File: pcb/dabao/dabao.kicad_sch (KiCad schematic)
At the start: 67 parts, among them J1 Conn_01x05, J2 USB_C_Receptacle_USB2.0_16P, J3 Conn_01x04, J4 MagConn_01x04_Pin, J5 Conn_Battery, J7 Conn_01x04, J8 Display, SW1 SW_RESET, SW2 SW_POWER, U1 nice_nano, U2 MCP23017_SP

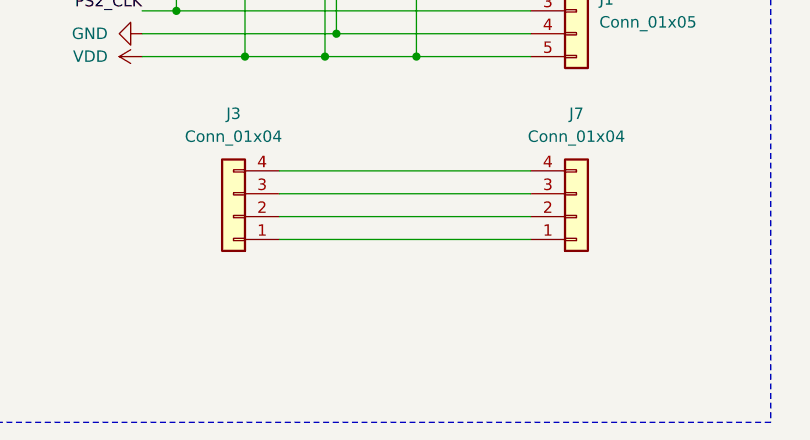
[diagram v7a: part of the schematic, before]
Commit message: Update outline for mounting holes
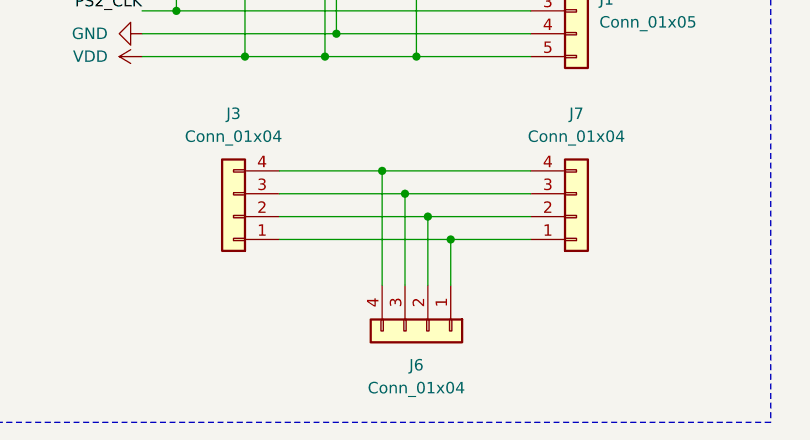
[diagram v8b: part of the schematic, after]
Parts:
- added J6: Conn_01x04, Library:TPSensorModule_Connector, symbol Connector_Generic:Conn_01x04
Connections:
- net at J3.1 (Pin_1), J7.1 (Pin_1): now also J6.1 (Pin_1)
- net at J3.2 (Pin_2), J7.2 (Pin_2): now also J6.2 (Pin_2)
- net at J3.3 (Pin_3), J7.3 (Pin_3): now also J6.3 (Pin_3)
- net at J3.4 (Pin_4), J7.4 (Pin_4): now also J6.4 (Pin_4)
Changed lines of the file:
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@@
 	)
 	(junction
+		(at 67.31 170.18)
+		(diameter 0)
+		(color 0 0 0 0)
+	)
+	(junction
 		(at 54.61 39.37)
 		(diameter 0)
@@
 	)
 	(junction
+		(at 64.77 167.64)
+		(diameter 0)
+		(color 0 0 0 0)
+	)
+	(junction
 		(at 46.99 152.4)
 		(diameter 0)
@@
 	)
 	(junction
+		(at 69.85 172.72)
+		(diameter 0)
+		(color 0 0 0 0)
+	)
+	(junction
 		(at 44.45 55.88)
 		(diameter 0)
@@
 	)
 	(junction
+		(at 62.23 165.1)
+		(diameter 0)
+		(color 0 0 0 0)
+	)
+	(junction
 		(at 59.69 52.07)
 		(diameter 0)
@@
 	(wire
 		(pts
-			(xy 50.8 172.72) (xy 78.74 172.72)
+			(xy 50.8 172.72) (xy 69.85 172.72)
 		)
 		(stroke
@@
 	(wire
 		(pts
+			(xy 67.31 170.18) (xy 78.74 170.18)
+		)
+		(stroke
+			(width 0)
+			(type default)
+		)
+	)
+	(wire
+		(pts
 			(xy 49.53 52.07) (xy 59.69 52.07)
 		)
@@
 	(wire
 		(pts
-			(xy 50.8 165.1) (xy 78.74 165.1)
+			(xy 62.23 177.8) (xy 62.23 165.1)
+		)
+		(stroke
+			(width 0)
+			(type default)
+		)
+	)
+	(wire
+		(pts
+			(xy 50.8 165.1) (xy 62.23 165.1)
 		)
 		(stroke
@@
 	(wire
 		(pts
+			(xy 64.77 167.64) (xy 64.77 177.8)
+		)
+		(stroke
+			(width 0)
+			(type default)
+		)
+	)
+	(wire
+		(pts
 			(xy 175.26 29.21) (xy 175.26 31.75)
 		)
@@
 	(wire
 		(pts
-			(xy 50.8 167.64) (xy 78.74 167.64)
+			(xy 50.8 167.64) (xy 64.77 167.64)
 		)
 		(stroke
@@
 	(wire
 		(pts
+			(xy 64.77 167.64) (xy 78.74 167.64)
+		)
+		(stroke
+			(width 0)
+			(type default)
+		)
+	)
+	(wire
+		(pts
 			(xy 80.01 101.6) (xy 90.17 101.6)
 		)
@@
 	(wire
 		(pts
-			(xy 50.8 170.18) (xy 78.74 170.18)
+			(xy 50.8 170.18) (xy 67.31 170.18)
 		)
 		(stroke
@@
 	(wire
 		(pts
+			(xy 62.23 165.1) (xy 78.74 165.1)
+		)
+		(stroke
+			(width 0)
+			(type default)
+		)
+	)
+	(wire
+		(pts
 			(xy 64.77 39.37) (xy 64.77 55.88)
 		)
@@
 	(wire
 		(pts
+			(xy 67.31 177.8) (xy 67.31 170.18)
+		)
+		(stroke
+			(width 0)
+			(type default)
+		)
+	)
+	(wire
+		(pts
 			(xy 69.85 52.07) (xy 80.01 52.07)
 		)
@@
 	(wire
 		(pts
+			(xy 69.85 172.72) (xy 69.85 177.8)
+		)
+		(stroke
+			(width 0)
+			(type default)
+		)
+	)
+	(wire
+		(pts
 			(xy 64.77 135.89) (xy 64.77 144.78)
 		)
@@
 	(wire
 		(pts
+			(xy 69.85 172.72) (xy 78.74 172.72)
+		)
+		(stroke
+			(width 0)
+			(type default)
+		)
+	)
+	(wire
+		(pts
 			(xy 184.15 76.2) (xy 189.23 76.2)
 		)
@@
 					(unit 1)
 				)
+			)
+		)
+	)
+	(symbol
+		(lib_id "Connector_Generic:Conn_01x04")
+		(at 67.31 182.88 270)
+		(unit 1)
+		(exclude_from_sim no)
+		(in_bom yes)
+		(on_board yes)
+		(dnp no)
+		(fields_autoplaced yes)
+		(property "Reference" "J6"
+			(at 66.04 186.69 90)
+			(effects
+				(font
+					(size 1.27 1.27)
+				)
+			)
+		)
+		(property "Value" "Conn_01x04"
+			(at 66.04 189.23 90)
+			(effects
+				(font
+					(size 1.27 1.27)
+				)
+			)
+		)
+		(property "Footprint" "Library:TPSensorModule_Connector"
+			(at 67.31 182.88 0)
+			(effects
+				(font
+					(size 1.27 1.27)
+				)
+				(hide yes)
+			)
+		)
+		(property "Datasheet" "~"
+			(at 67.31 182.88 0)
+			(effects
+				(font
+					(size 1.27 1.27)
+				)
+				(hide yes)
+			)
+		)
+		(property "Description" "Generic connector, single row, 01x04, script generated (kicad-library-utils/schlib/autogen/connector/)"
+			(at 67.31 182.88 0)
+			(effects
+				(font
+					(size 1.27 1.27)
+				)
+				(hide yes)
+			)
+		)
+		(pin "4"
+		)
+		(pin "1"
+		)
+		(pin "3"
+		)
+		(pin "2"
+		)
+		(instances
+			(project "dabao"
+				(path "/f7dfc45c-83ad-43c7-9815-463af0b28fbd"
+					(reference "J6")
+					(unit 1)
+				)
